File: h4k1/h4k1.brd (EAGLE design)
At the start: 250 x 80 mm, 198 parts, among them IC1 STM32F10XCXT6, J2 PJ-313D-AUDIO-JACK, J3 USB-AF10, K1 CHERRY-MX-LED, K10 CHERRY-MX, K11 CHERRY-MX, K12 CHERRY-MX, K13 CHERRY-MX, K14 CHERRY-MX, K15 CHERRY-MX, K16 CHERRY-MX, K17 CHERRY-MX-LED, K18 CHERRY-MX, K19 CHERRY-MX, K2 CHERRY-MX-LED, K20 CHERRY-MX, K21 CHERRY-MX, K22 CHERRY-MX, K23 CHERRY-MX, K24 CHERRY-MX, K25 CHERRY-MX-LED, K26 CHERRY-MX, K27 CHERRY-MX, K28 CHERRY-MX, K29 CHERRY-MX, K3 CHERRY-MX-LED, K30 CHERRY-MX, K31 CHERRY-MX, K32 CHERRY-MX, K33 CHERRY-MX-LED, K34 CHERRY-MX, K35 CHERRY-MX, K36 CHERRY-MX-LED, K37 CHERRY-MX-LED, K38 CHERRY-MX, K39 CHERRY-MX, K4 CHERRY-MX-LED, K40 CHERRY-MX-LED, K41 CHERRY-MX, K42 CHERRY-MX, K43 CHERRY-MX, K44 CHERRY-MX, K45 CHERRY-MX, K46 CHERRY-MX-LED, K5 CHERRY-MX-LED, K6 CHERRY-MX-LED, K65 EVQPUL02K, K66 EVQPUL02K, K67 K3-1280S-F2, K7 CHERRY-MX-LED, K8 CHERRY-MX-LED, K9 CHERRY-MX-LED, T1 DBG, U1 GL850G, U3 PCM2704CDB, X3 12MHz, X4 12MHz

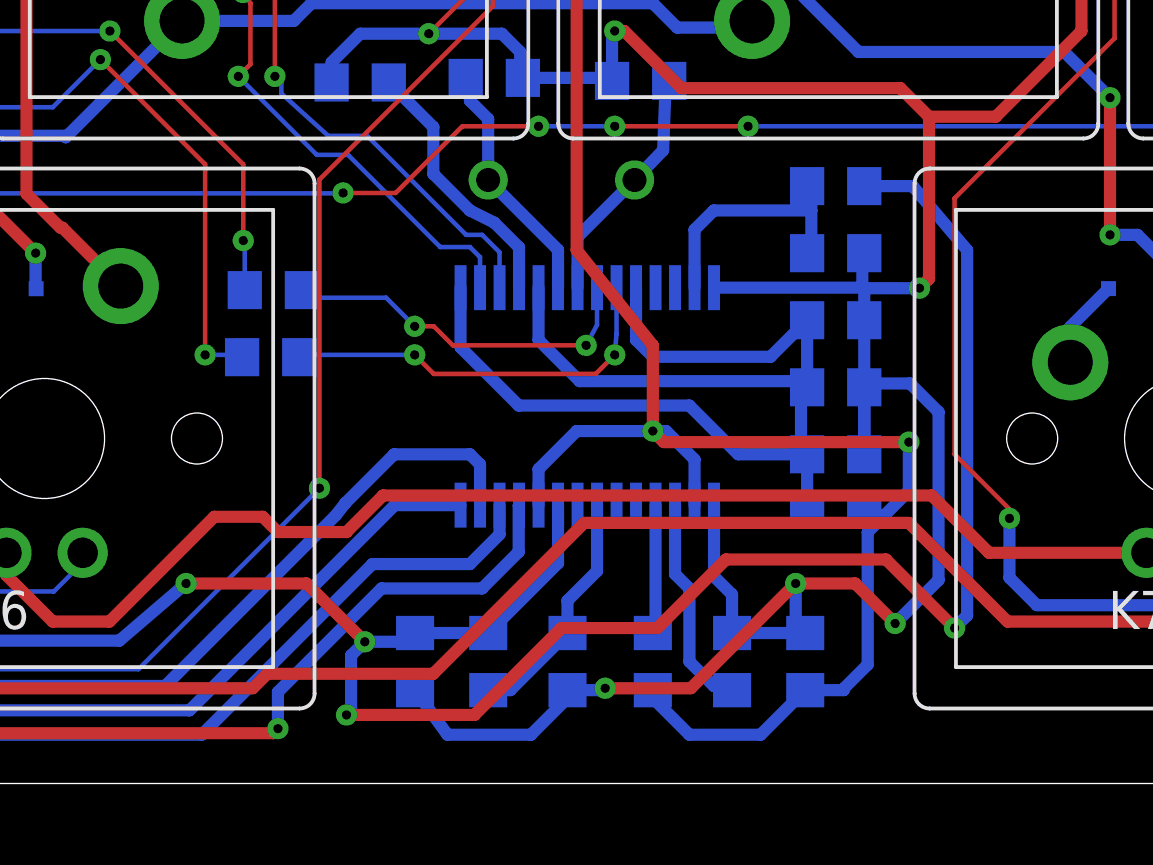
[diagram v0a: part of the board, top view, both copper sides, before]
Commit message: update keybord for gl850 not limit power usage
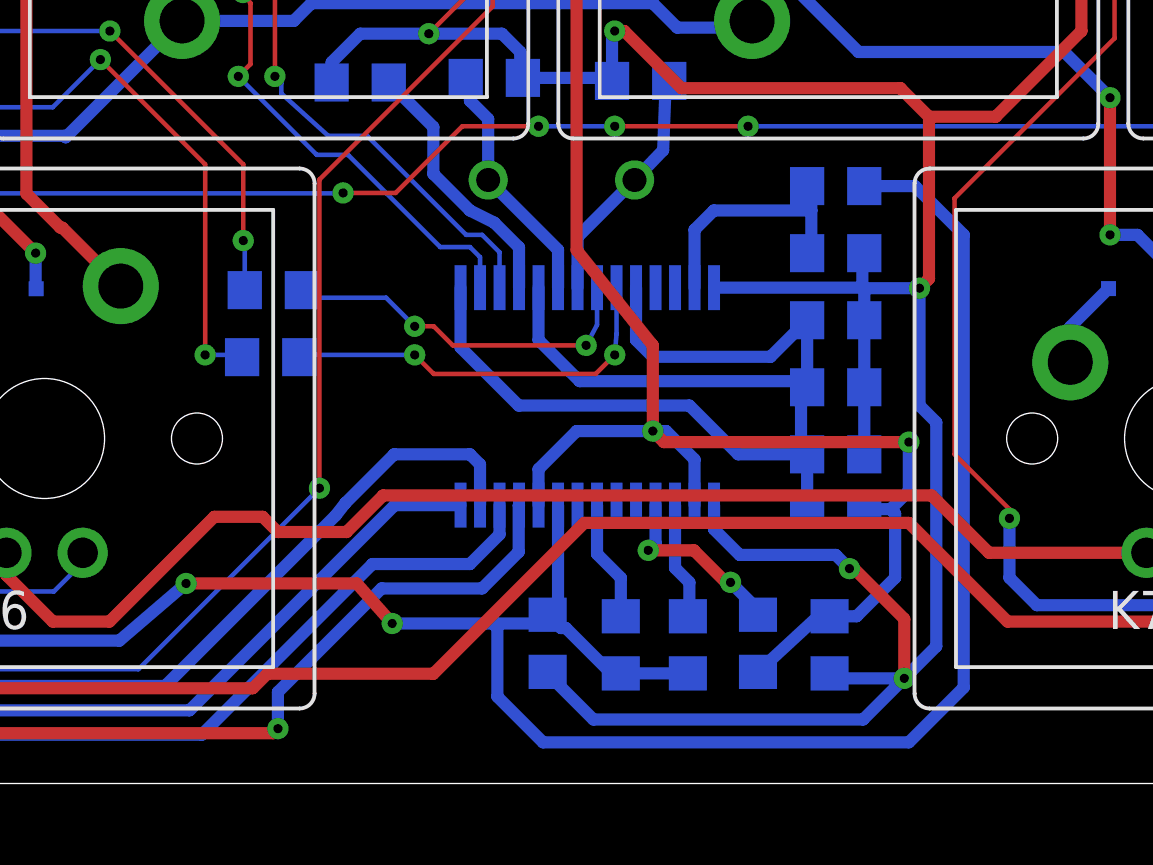
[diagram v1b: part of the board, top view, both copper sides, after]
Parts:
- removed R24: 10k, hqc:0805
- R22, R23, R25: value 10k -> 100k
- moved C17 4.46 mm to (148.9, 4.67)
- moved R25 4.45 mm to (151.3, 4.62), turned to 270 degrees
- moved R22 3.56 mm to (155.9, 4.67)
- moved R23 1.58 mm to (153.6, 4.62), turned to 270 degrees
- moved C19 0.99 mm to (158.3, 4.62), turned to 90 degrees
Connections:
- net 5V: now also R23.P$2
- net GND: no longer R23.P$2, R24.P$2
- net N$34: no longer R24.P$1
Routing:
- net VDD: track 339.9 -> 334.1 mm
- net N$34: track 8.10 -> 4.03 mm
- net N$30: track 7.23 -> 3.92 mm
- net N$28: track 4.30 -> 6.25 mm, vias 0 -> 2
- net GND: track 647.4 -> 645.9 mm, vias 31 -> 30
- net 5V: track 181.6 -> 182.3 mm, vias 8 -> 6

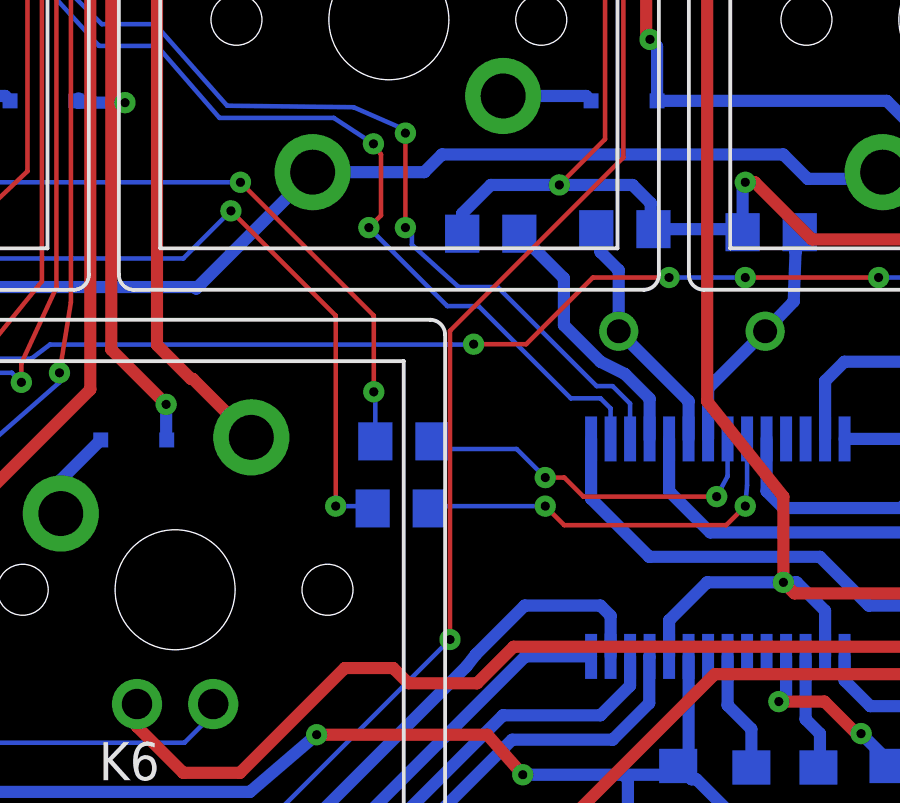
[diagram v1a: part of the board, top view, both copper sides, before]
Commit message: add usb pull up resistor
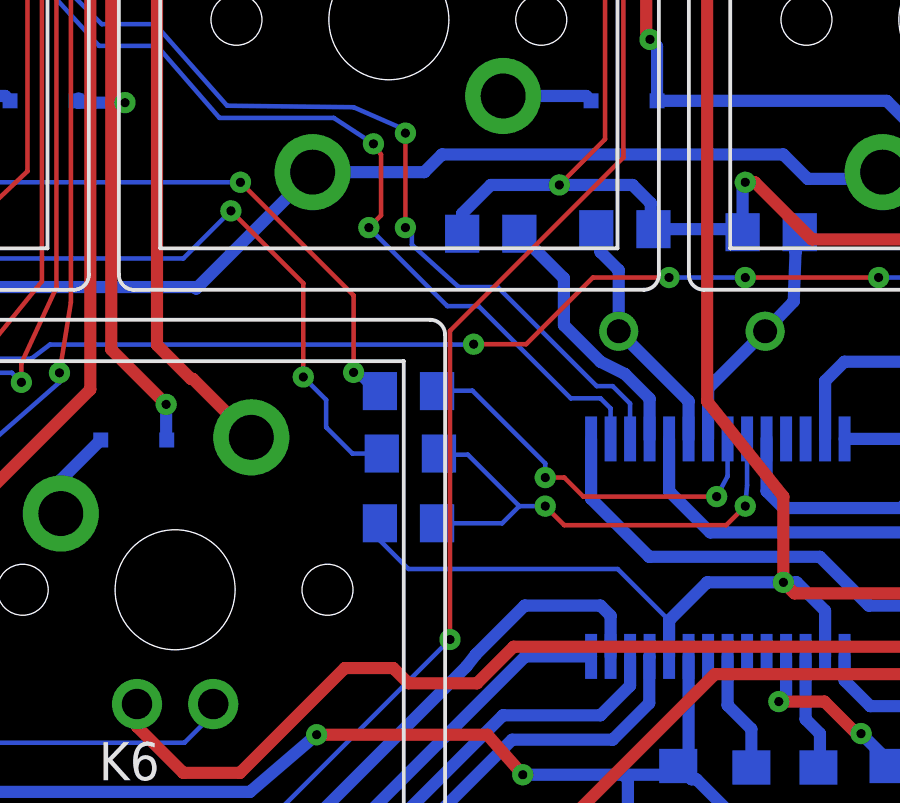
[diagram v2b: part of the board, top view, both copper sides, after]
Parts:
- added R24: 1.5k, hqc:0805
- moved R38 1.85 mm to (140.0, 16.0)
- moved R37 1.68 mm to (139.9, 18.1)
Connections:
- net USB3+: now also R24.P$2
- net VDD: now also R24.P$1
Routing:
- net VDD: track 334.1 -> 345.5 mm
- net USB3+: track 13.3 -> 16.7 mm
- net N$74: track 42.1 -> 40.3 mm
- net N$72: track 41.0 -> 39.5 mm
- net USB3-: track 12.3 -> 13.1 mm
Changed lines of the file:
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@@
 <attribute name="VALUE" x="116.25" y="74.3103" size="1.27" layer="28" rot="MR90"/>
 </element>
-<element name="R37" library="hqc" package="0805" value="15" x="139.7508" y="16.4465" smashed="yes" rot="MR180">
-<attribute name="NAME" x="141.4526" y="17.145" size="1.27" layer="26" rot="MR180"/>
-<attribute name="VALUE" x="136.2583" y="20.2565" size="1.27" layer="28" rot="MR180"/>
+<element name="R37" library="hqc" package="0805" value="15" x="139.9032" y="18.1229" smashed="yes" rot="MR180">
+<attribute name="NAME" x="141.605" y="18.8214" size="1.27" layer="26" rot="MR180"/>
+<attribute name="VALUE" x="136.4107" y="21.9329" size="1.27" layer="28" rot="MR180"/>
 </element>
-<element name="R38" library="hqc" package="0805" value="15" x="139.6619" y="14.2113" smashed="yes" rot="MR180">
-<attribute name="NAME" x="141.5161" y="14.9098" size="1.27" layer="26" rot="MR180"/>
-<attribute name="VALUE" x="136.1694" y="18.0213" size="1.27" layer="28" rot="MR180"/>
+<element name="R38" library="hqc" package="0805" value="15" x="139.9667" y="16.0401" smashed="yes" rot="MR180">
+<attribute name="NAME" x="141.8209" y="16.7386" size="1.27" layer="26" rot="MR180"/>
+<attribute name="VALUE" x="136.4742" y="19.8501" size="1.27" layer="28" rot="MR180"/>
 </element>
 <element name="R39" library="hqc" package="0805" value="200" x="97.1042" y="71.7804" smashed="yes" rot="MR90">
@@
 <element name="U$7" library="hqc" package="M2-MOUNTING-HOLE" value="M2-MOUNTING-HOLE" x="182" y="20"/>
 <element name="U$8" library="hqc" package="M2-MOUNTING-HOLE" value="M2-MOUNTING-HOLE" x="78.3476" y="67"/>
+<element name="R24" library="hqc" package="0805" value="1.5k" x="139.9032" y="13.716" rot="MR180"/>
 </elements>
 <signals>
@@
 <wire x1="158.2928" y1="5.5753" x2="157.9118" y2="5.5753" width="0.4064" layer="16"/>
 <wire x1="157.9118" y1="5.5753" x2="155.9052" y2="3.7211" width="0.4064" layer="16"/>
+<contactref element="R24" pad="P$1"/>
+<wire x1="138.9507" y1="13.716" x2="138.9507" y2="13.1445" width="0.1524" layer="16"/>
+<wire x1="138.9507" y1="13.1445" x2="139.9032" y2="12.192" width="0.1524" layer="16"/>
+<wire x1="139.9032" y1="12.192" x2="146.8767" y2="12.192" width="0.1524" layer="16"/>
+<wire x1="146.8767" y1="12.192" x2="148.5906" y2="10.4781" width="0.1524" layer="16"/>
 </signal>
 <signal name="KB_C1">
@@
 <wire x1="145.0975" y1="15.24" x2="144.4625" y2="15.24" width="0.1524" layer="1"/>
 <via x="144.4625" y="15.24" extent="1-16" drill="0.3048"/>
-<wire x1="144.4625" y1="15.24" x2="143.51" y2="16.1925" width="0.1524" layer="16"/>
-<wire x1="143.51" y1="16.1925" x2="140.9573" y2="16.1925" width="0.1524" layer="16"/>
-<wire x1="140.9573" y1="16.1925" x2="140.7033" y2="16.4465" width="0.1524" layer="16"/>
+<wire x1="144.4625" y1="15.24" x2="144.4625" y2="15.7099" width="0.1524" layer="16"/>
+<wire x1="144.4625" y1="15.7099" x2="142.0368" y2="18.1356" width="0.1524" layer="16"/>
+<wire x1="142.0368" y1="18.1356" x2="140.8684" y2="18.1356" width="0.1524" layer="16"/>
+<wire x1="140.8684" y1="18.1356" x2="140.8557" y2="18.1229" width="0.1524" layer="16"/>
 </signal>
 <signal name="USB3+">
@@
 <via x="151.13" y="14.2875" extent="1-16" drill="0.3048"/>
 <via x="144.4625" y="14.2875" extent="1-16" drill="0.3048"/>
-<wire x1="144.4625" y1="14.2875" x2="140.6906" y2="14.2875" width="0.1524" layer="16"/>
-<wire x1="140.6906" y1="14.2875" x2="140.6144" y2="14.2113" width="0.1524" layer="16"/>
 <wire x1="151.13" y1="14.2875" x2="150.495" y2="13.6525" width="0.1524" layer="1"/>
 <wire x1="150.495" y1="13.6525" x2="145.0975" y2="13.6525" width="0.1524" layer="1"/>
 <wire x1="145.0975" y1="13.6525" x2="144.4625" y2="14.2875" width="0.1524" layer="1"/>
+<contactref element="R24" pad="P$2"/>
+<wire x1="144.4625" y1="14.2875" x2="143.5989" y2="14.2875" width="0.1524" layer="16"/>
+<wire x1="143.5989" y1="14.2875" x2="141.8844" y2="16.002" width="0.1524" layer="16"/>
+<wire x1="141.8844" y1="16.002" x2="140.9573" y2="16.002" width="0.1524" layer="16"/>
+<wire x1="140.9573" y1="16.002" x2="140.9192" y2="16.0401" width="0.1524" layer="16"/>
+<wire x1="140.8557" y1="13.716" x2="143.0274" y2="13.716" width="0.1524" layer="16"/>
+<wire x1="143.0274" y1="13.716" x2="143.5989" y2="14.2875" width="0.1524" layer="16"/>
 </signal>
 <signal name="USB4-">
@@
 <contactref element="IC1" pad="32"/>
 <contactref element="R37" pad="P$1"/>
-<wire x1="138.7983" y1="16.4465" x2="138.7983" y2="18.0467" width="0.1524" layer="16"/>
-<wire x1="138.7983" y1="18.0467" x2="138.7475" y2="18.0975" width="0.1524" layer="16"/>
-<via x="138.7475" y="18.0975" extent="1-16" drill="0.3048"/>
-<wire x1="138.7475" y1="18.0975" x2="138.7475" y2="20.6375" width="0.1524" layer="1"/>
-<wire x1="138.7475" y1="20.6375" x2="134.3025" y2="25.0825" width="0.1524" layer="1"/>
 <via x="134.3025" y="25.0825" extent="1-16" drill="0.3048"/>
 <wire x1="134.3025" y1="25.0825" x2="124.1425" y2="25.0825" width="0.1524" layer="16"/>
@@
 <wire x1="113.538" y1="25.4508" x2="114.7325" y2="24.3325" width="0.1524" layer="16"/>
 <wire x1="114.7325" y1="22.534" x2="114.7325" y2="24.3325" width="0.1524" layer="16"/>
+<wire x1="138.9507" y1="18.1229" x2="138.6967" y2="18.1229" width="0.1524" layer="16"/>
+<wire x1="138.6967" y1="18.1229" x2="138.0744" y2="18.7452" width="0.1524" layer="16"/>
+<via x="138.0744" y="18.7452" extent="1-16" drill="0.3048"/>
+<wire x1="138.0744" y1="18.7452" x2="138.0744" y2="21.3106" width="0.1524" layer="1"/>
+<wire x1="138.0744" y1="21.3106" x2="134.3025" y2="25.0825" width="0.1524" layer="1"/>
 </signal>
 <signal name="N$74">
@@
 <wire x1="132.3975" y1="22.5425" x2="133.985" y2="24.13" width="0.1524" layer="16"/>
 <via x="133.985" y="24.13" extent="1-16" drill="0.3048"/>
-<wire x1="133.985" y1="24.13" x2="137.4775" y2="20.6375" width="0.1524" layer="1"/>
-<wire x1="137.4775" y1="20.6375" x2="137.4775" y2="14.2875" width="0.1524" layer="1"/>
-<via x="137.4775" y="14.2875" extent="1-16" drill="0.3048"/>
-<wire x1="137.4775" y1="14.2875" x2="138.6332" y2="14.2875" width="0.1524" layer="16"/>
-<wire x1="138.6332" y1="14.2875" x2="138.7094" y2="14.2113" width="0.1524" layer="16"/>
+<wire x1="133.985" y1="24.13" x2="136.398" y2="21.717" width="0.1524" layer="1"/>
 <wire x1="113.665" y1="28.2448" x2="113.792" y2="28.2448" width="0.1524" layer="16"/>
 <wire x1="113.792" y1="28.2448" x2="114.1476" y2="27.8892" width="0.1524" layer="16"/>
@@
 <wire x1="119.634" y1="26.0604" x2="122.0597" y2="26.0604" width="0.1524" layer="16"/>
 <wire x1="122.0597" y1="26.0604" x2="125.73" y2="22.5425" width="0.1524" layer="16"/>
+<wire x1="139.0142" y1="16.0401" x2="138.0363" y2="16.0401" width="0.1524" layer="16"/>
+<wire x1="138.0363" y1="16.0401" x2="137.16" y2="16.9164" width="0.1524" layer="16"/>
+<wire x1="137.16" y1="16.9164" x2="137.16" y2="17.8308" width="0.1524" layer="16"/>
+<wire x1="137.16" y1="17.8308" x2="136.398" y2="18.5928" width="0.1524" layer="16"/>
+<via x="136.398" y="18.5928" extent="1-16" drill="0.3048"/>
+<wire x1="136.398" y1="18.5928" x2="136.398" y2="21.717" width="0.1524" layer="1"/>
 </signal>
 <signal name="LED_R4">
